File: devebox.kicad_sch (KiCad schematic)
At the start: 27 parts, among them J1 ST-LINK, J2 USB, SW1 RESET SW, U3 STM32H743VITx, U4 W25Q128, Y1 25MHZ

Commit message: snapshot
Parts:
- C12, C13, C16, C17, C18, C19, C20, C21, C22: footprint Capacitor_SMD:C_0603_1608Metric_Pad1.08x0.95mm_HandSolder -> EggClassifier:C_0805_2012Metric_Pad1.18x1.45mm_HandSolder
- C14, C15: footprint Capacitor_SMD:C_0805_2012Metric_Pad1.18x1.45mm_HandSolder -> EggClassifier:C_0805_2012Metric_Pad1.18x1.45mm_HandSolder
- D6: footprint LED_SMD:LED_0805_2012Metric_Pad1.15x1.40mm_HandSolder -> EggClassifier:LED_0805_2012Metric_Pad1.15x1.40mm_HandSolder
- J1: footprint Connector_PinHeader_2.54mm:PinHeader_1x05_P2.54mm_Vertical -> EggClassifier:PinHeader_1x05_P2.54mm_Vertical
- J2: footprint Connector_PinHeader_2.54mm:PinHeader_1x04_P2.54mm_Vertical -> EggClassifier:PinHeader_1x04_P2.54mm_Vertical
- R12, R13, R14, R15, R16, R17, R18, R19, R20: footprint Resistor_SMD:R_0805_2012Metric_Pad1.20x1.40mm_HandSolder -> EggClassifier:R_0805_2012Metric_Pad1.20x1.40mm_HandSolder
- SW1: footprint Button_Switch_THT:SW_PUSH_6mm_H4.3mm -> EggClassifier:SW_PUSH_6mm_H4.3mm
- U3: footprint Package_QFP:LQFP-100_14x14mm_P0.5mm -> EggClassifier:LQFP-100_14x14mm_P0.5mm
- U4: footprint PCM_JLCPCB:SOIC-8_L5.3-W5.3-P1.27-LS8.0-BL -> EggClassifier:SOIC-8_L5.3-W5.3-P1.27-LS8.0-BL
- Y1: footprint Oscillator:Oscillator_SMD_Abracon_ASV-4Pin_7.0x5.1mm_HandSoldering -> EggClassifier:Oscillator_SMD_Abracon_ASV-4Pin_7.0x5.1mm_HandSoldering
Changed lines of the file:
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@@
 			)
 		)
-		(property "Footprint" "Resistor_SMD:R_0805_2012Metric_Pad1.20x1.40mm_HandSolder"
+		(property "Footprint" "EggClassifier:R_0805_2012Metric_Pad1.20x1.40mm_HandSolder"
 			(at 167.64 95.25 0)
 			(effects
@@
 			)
 		)
-		(property "Footprint" "Capacitor_SMD:C_0603_1608Metric_Pad1.08x0.95mm_HandSolder"
+		(property "Footprint" "EggClassifier:C_0805_2012Metric_Pad1.18x1.45mm_HandSolder"
 			(at 252.73 81.5848 0)
 			(effects
@@
 			)
 		)
-		(property "Footprint" "Capacitor_SMD:C_0805_2012Metric_Pad1.18x1.45mm_HandSolder"
+		(property "Footprint" "EggClassifier:C_0805_2012Metric_Pad1.18x1.45mm_HandSolder"
 			(at 73.3552 158.75 0)
 			(effects
@@
 			)
 		)
-		(property "Footprint" "Resistor_SMD:R_0805_2012Metric_Pad1.20x1.40mm_HandSolder"
+		(property "Footprint" "EggClassifier:R_0805_2012Metric_Pad1.20x1.40mm_HandSolder"
 			(at 153.67 77.47 0)
 			(effects
@@
 			)
 		)
-		(property "Footprint" "Capacitor_SMD:C_0603_1608Metric_Pad1.08x0.95mm_HandSolder"
+		(property "Footprint" "EggClassifier:C_0805_2012Metric_Pad1.18x1.45mm_HandSolder"
 			(at 26.67 44.1452 0)
 			(effects
@@
 			)
 		)
-		(property "Footprint" "Resistor_SMD:R_0805_2012Metric_Pad1.20x1.40mm_HandSolder"
+		(property "Footprint" "EggClassifier:R_0805_2012Metric_Pad1.20x1.40mm_HandSolder"
 			(at 171.45 127 0)
 			(effects
@@
 			)
 		)
-		(property "Footprint" "Resistor_SMD:R_0805_2012Metric_Pad1.20x1.40mm_HandSolder"
+		(property "Footprint" "EggClassifier:R_0805_2012Metric_Pad1.20x1.40mm_HandSolder"
 			(at 63.5 53.34 0)
 			(effects
@@
 			)
 		)
-		(property "Footprint" "Capacitor_SMD:C_0603_1608Metric_Pad1.08x0.95mm_HandSolder"
+		(property "Footprint" "EggClassifier:C_0805_2012Metric_Pad1.18x1.45mm_HandSolder"
 			(at 199.0852 34.29 0)
 			(effects
@@
 			)
 		)
-		(property "Footprint" "Capacitor_SMD:C_0603_1608Metric_Pad1.08x0.95mm_HandSolder"
+		(property "Footprint" "EggClassifier:C_0805_2012Metric_Pad1.18x1.45mm_HandSolder"
 			(at 52.07 39.0652 0)
 			(effects
@@
 			)
 		)
-		(property "Footprint" "Resistor_SMD:R_0805_2012Metric_Pad1.20x1.40mm_HandSolder"
+		(property "Footprint" "EggClassifier:R_0805_2012Metric_Pad1.20x1.40mm_HandSolder"
 			(at 153.67 67.31 0)
 			(effects
@@
 			)
 		)
-		(property "Footprint" "Package_QFP:LQFP-100_14x14mm_P0.5mm"
+		(property "Footprint" "EggClassifier:LQFP-100_14x14mm_P0.5mm"
 			(at 80.01 167.64 0)
 			(effects
@@
 			)
 		)
-		(property "Footprint" "Capacitor_SMD:C_0603_1608Metric_Pad1.08x0.95mm_HandSolder"
+		(property "Footprint" "EggClassifier:C_0805_2012Metric_Pad1.18x1.45mm_HandSolder"
 			(at 188.9252 34.29 0)
 			(effects
@@
 			)
 		)
-		(property "Footprint" "Oscillator:Oscillator_SMD_Abracon_ASV-4Pin_7.0x5.1mm_HandSoldering"
+		(property "Footprint" "EggClassifier:Oscillator_SMD_Abracon_ASV-4Pin_7.0x5.1mm_HandSoldering"
 			(at 41.91 62.23 0)
 			(effects
@@
 			)
 		)
-		(property "Footprint" "Resistor_SMD:R_0805_2012Metric_Pad1.20x1.40mm_HandSolder"
+		(property "Footprint" "EggClassifier:R_0805_2012Metric_Pad1.20x1.40mm_HandSolder"
 			(at 167.64 97.79 0)
 			(effects
@@
 			)
 		)
-		(property "Footprint" "Capacitor_SMD:C_0603_1608Metric_Pad1.08x0.95mm_HandSolder"
+		(property "Footprint" "EggClassifier:C_0805_2012Metric_Pad1.18x1.45mm_HandSolder"
 			(at 178.7652 34.29 0)
 			(effects
@@
 			)
 		)
-		(property "Footprint" "Button_Switch_THT:SW_PUSH_6mm_H4.3mm"
+		(property "Footprint" "EggClassifier:SW_PUSH_6mm_H4.3mm"
 			(at 55.88 39.37 0)
 			(effects
@@
 			)
 		)
-		(property "Footprint" "Connector_PinHeader_2.54mm:PinHeader_1x04_P2.54mm_Vertical"
+		(property "Footprint" "EggClassifier:PinHeader_1x04_P2.54mm_Vertical"
 			(at 180.34 95.25 0)
 			(effects
@@
 			)
 		)
-		(property "Footprint" "Capacitor_SMD:C_0805_2012Metric_Pad1.18x1.45mm_HandSolder"
+		(property "Footprint" "EggClassifier:C_0805_2012Metric_Pad1.18x1.45mm_HandSolder"
 			(at 67.0052 158.75 0)
 			(effects
@@
 			)
 		)
-		(property "Footprint" "Resistor_SMD:R_0805_2012Metric_Pad1.20x1.40mm_HandSolder"
+		(property "Footprint" "EggClassifier:R_0805_2012Metric_Pad1.20x1.40mm_HandSolder"
 			(at 59.69 43.18 0)
 			(effects
@@
 			)
 		)
-		(property "Footprint" "Connector_PinHeader_2.54mm:PinHeader_1x05_P2.54mm_Vertical"
+		(property "Footprint" "EggClassifier:PinHeader_1x05_P2.54mm_Vertical"
 			(at 171.45 68.58 0)
 			(effects
@@
 			)
 		)
-		(property "Footprint" "Capacitor_SMD:C_0603_1608Metric_Pad1.08x0.95mm_HandSolder"
+		(property "Footprint" "EggClassifier:C_0805_2012Metric_Pad1.18x1.45mm_HandSolder"
 			(at 204.1652 34.29 0)
 			(effects
@@
 			)
 		)
-		(property "Footprint" "PCM_JLCPCB:SOIC-8_L5.3-W5.3-P1.27-LS8.0-BL"
+		(property "Footprint" "EggClassifier:SOIC-8_L5.3-W5.3-P1.27-LS8.0-BL"
 			(at 228.6 101.6 0)
 			(effects
@@
 			)
 		)
-		(property "Footprint" "LED_SMD:LED_0805_2012Metric_Pad1.15x1.40mm_HandSolder"
+		(property "Footprint" "EggClassifier:LED_0805_2012Metric_Pad1.15x1.40mm_HandSolder"
 			(at 171.45 134.62 0)
 			(effects
@@
 			)
 		)
-		(property "Footprint" "Resistor_SMD:R_0805_2012Metric_Pad1.20x1.40mm_HandSolder"
+		(property "Footprint" "EggClassifier:R_0805_2012Metric_Pad1.20x1.40mm_HandSolder"
 			(at 72.39 31.75 0)
 			(effects
@@
 			)
 		)
-		(property "Footprint" "Resistor_SMD:R_0805_2012Metric_Pad1.20x1.40mm_HandSolder"
+		(property "Footprint" "EggClassifier:R_0805_2012Metric_Pad1.20x1.40mm_HandSolder"
 			(at 173.99 88.9 0)
 			(effects
@@
 			)
 		)
-		(property "Footprint" "Capacitor_SMD:C_0603_1608Metric_Pad1.08x0.95mm_HandSolder"
+		(property "Footprint" "EggClassifier:C_0805_2012Metric_Pad1.18x1.45mm_HandSolder"
 			(at 183.8452 34.29 0)
 			(effects
@@
 			)
 		)
-		(property "Footprint" "Capacitor_SMD:C_0603_1608Metric_Pad1.08x0.95mm_HandSolder"
+		(property "Footprint" "EggClassifier:C_0805_2012Metric_Pad1.18x1.45mm_HandSolder"
 			(at 194.0052 34.29 0)
 			(effects

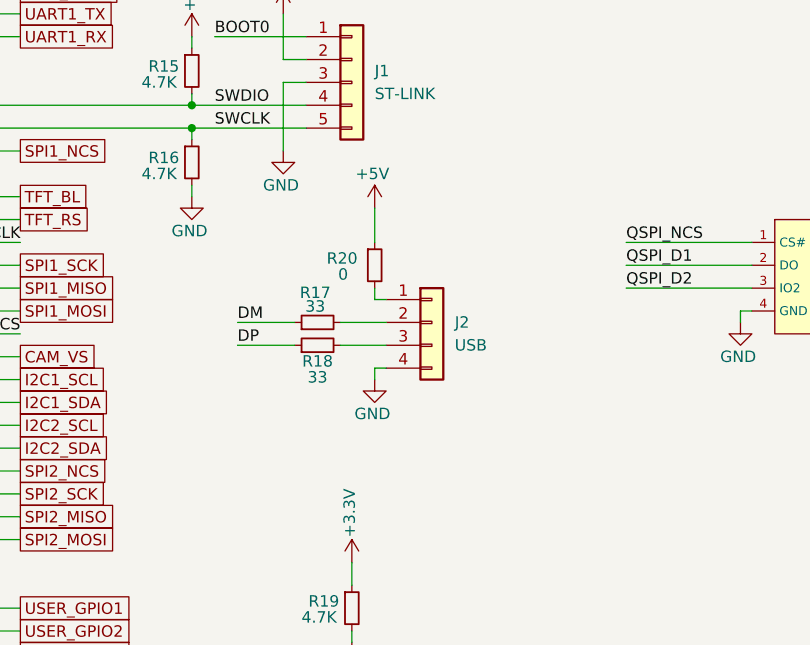
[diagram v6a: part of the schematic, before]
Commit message: change board to dimensions 120mm x 80mm
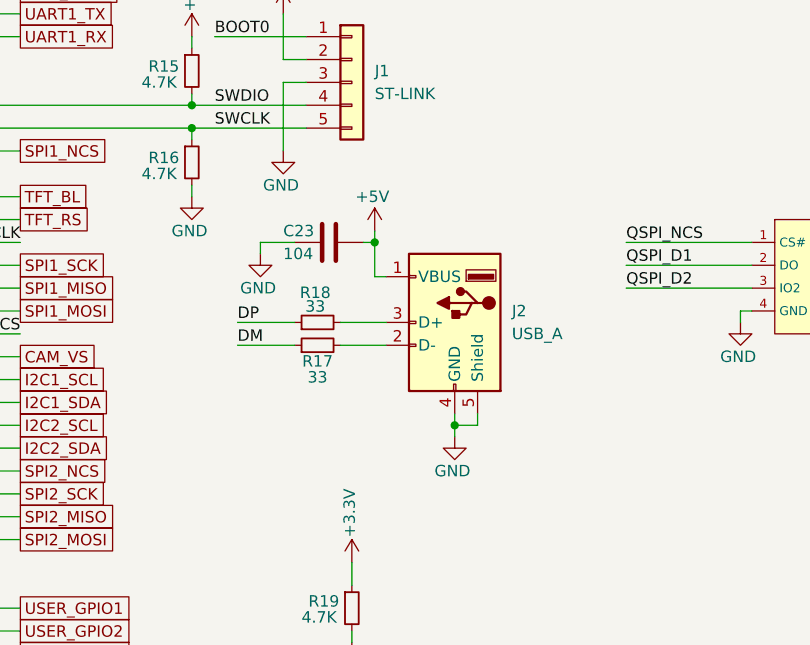
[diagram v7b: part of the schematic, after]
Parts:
- removed J2: USB, EggClassifier:PinHeader_1x04_P2.54mm_Vertical, symbol EggClassifier:Conn_01x04_1
- removed R20: 0, EggClassifier:R_0805_2012Metric_Pad1.20x1.40mm_HandSolder, symbol EggClassifier:R_Small
- added C23: 104, EggClassifier:C_0805_2012Metric_Pad1.18x1.45mm_HandSolder, symbol EggClassifier:C
- added J2: USB_A, EggClassifier:USB_A_Molex_67643_Horizontal, symbol Connector:USB_A
- renumbered R18 to R17, R17 to R18
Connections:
- net +5V: now also C23.1, J2.1 (VBUS)
- net DM: now also R17.1; no longer R18.1
- net DP: now also R18.1; no longer R17.1
- net GND: now also C23.2, J2.4 (GND), J2.5 (Shield)
- net at R18.2: now also J2.3 (D+)
- net at R17.2: now also J2.2 (D-)

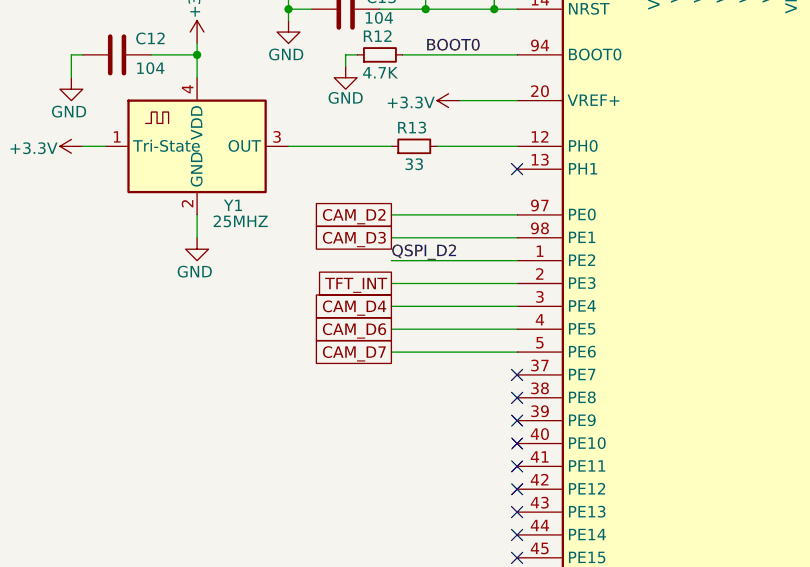
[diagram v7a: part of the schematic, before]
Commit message: finished layout;. H743 with SD-Card
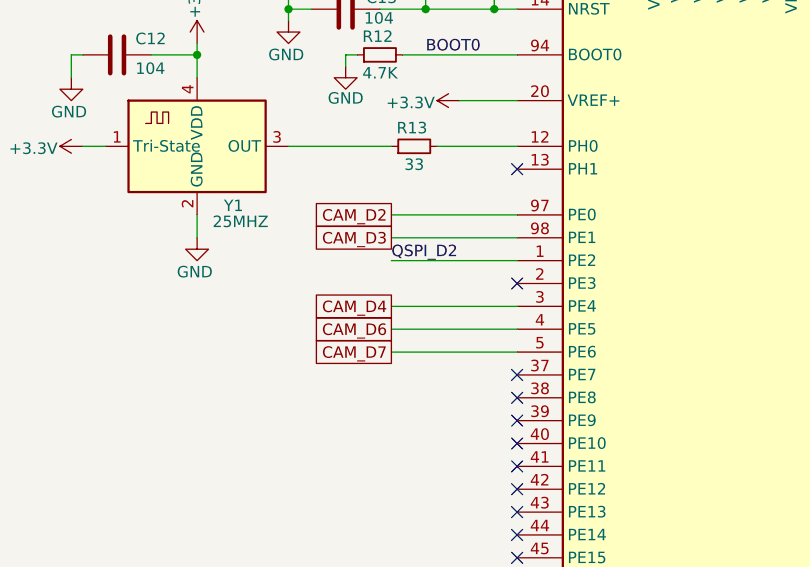
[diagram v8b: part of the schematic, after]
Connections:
- net TFT_INT: no longer names the net of U3.2 (PE3)
- no-connect marks 28 -> 29
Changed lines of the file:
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@@
+	)
+	(no_connect
+		(at 74.93 68.58)
 	)
 	(no_connect
@@
 		(pts
 			(xy 120.65 66.04) (xy 129.54 66.04)
-		)
-		(stroke
-			(width 0)
-			(type default)
-		)
-	)
-	(wire
-		(pts
-			(xy 60.96 68.58) (xy 74.93 68.58)
 		)
 		(stroke
@@
 				(hide yes)
 			)
-		)
-	)
-	(global_label "TFT_INT"
-		(shape passive)
-		(at 60.96 68.58 180)
-		(fields_autoplaced yes)
-		(effects
-			(font
-				(size 1.27 1.27)
-			)
-			(justify right)
-		)
-		(property "Intersheetrefs" "${INTERSHEET_REFS}"
-			(at 49.9692 68.58 0)
-			(effects
-				(font
-					(size 1.27 1.27)
-				)
-				(justify right)
-				(hide yes)
-			)
